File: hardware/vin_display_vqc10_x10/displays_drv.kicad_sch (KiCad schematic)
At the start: 38 parts, among them Q2 DMP2022LSS, Q3 DMP2022LSS, Q4 DMP2022LSS, Q5 DMP2022LSS, Q6 DMP2022LSS, Q8 DMP2022LSS, Q9 DMP2022LSS, U14 74HCT154, U15 74HCT154, U16 74HCT154

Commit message: routing vqc10_x10
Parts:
- removed C28, C29, C30, C31, C32, C38, C39, C40, C41, C42: 0.1u, Capacitor_SMD:C_0603_1608Metric, symbol Device:C
- R14: footprint (none) -> Capacitor_SMD:C_0603_1608Metric
- U14, U15, U16: footprint (none) -> Package_SO:TSSOP-24_4.4x7.8mm_P0.65mm
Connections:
- net DISP_C17: no longer U16.1 (Y0)
- net DISP_C18: no longer U16.2 (Y1)
- net DISP_C19: no longer U16.3 (Y2)
- net DISP_C20: no longer U16.4 (Y3)
- net DISP_C21: no longer U16.5 (Y4)
- net DISP_C22: no longer U16.6 (Y5)
- net DISP_C23: no longer U16.7 (Y6)
- net DISP_C24: no longer U16.8 (Y7)
- new net DISP_C33: U16.1 (Y0)
- new net DISP_C34: U16.2 (Y1)
- new net DISP_C35: U16.3 (Y2)
- new net DISP_C36: U16.4 (Y3)
- new net DISP_C37: U16.5 (Y4)
- new net DISP_C38: U16.6 (Y5)
- new net DISP_C39: U16.7 (Y6)
- new net DISP_C40: U16.8 (Y7)
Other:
- moved on the sheet: C23, C24, C25, C26, C27, C33, C34, C35, C36, C37

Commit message: route vqc10_x10 board
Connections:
- net DISP_VCC: now also U14.24 (VCC), U15.24 (VCC), U16.24 (VCC)
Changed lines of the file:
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@@
   (junction (at 250.19 97.79) (diameter 0) (color 0 0 0 0)
   )
+  (junction (at 63.5 114.3) (diameter 0) (color 0 0 0 0)
+  )
   (junction (at 73.66 84.455) (diameter 0) (color 0 0 0 0)
   )
@@
   )
   (wire (pts (xy 127.635 50.8) (xy 127.635 53.34))
+    (stroke (width 0) (type default))
+  )
+  (wire (pts (xy 63.5 114.3) (xy 78.74 114.3))
     (stroke (width 0) (type default))
   )
@@
       (effects (font (size 1.27 1.27)) (justify left) hide)
     )
+  )
+  (global_label "DISP_VCC" (shape input) (at 78.74 114.3 0) (fields_autoplaced)
+    (effects (font (size 1.27 1.27)) (justify left))
+    (property "Intersheetrefs" "${INTERSHEET_REFS}" (at 90.6757 114.3 0)
+      (effects (font (size 1.27 1.27)) (justify left) hide)
+    )

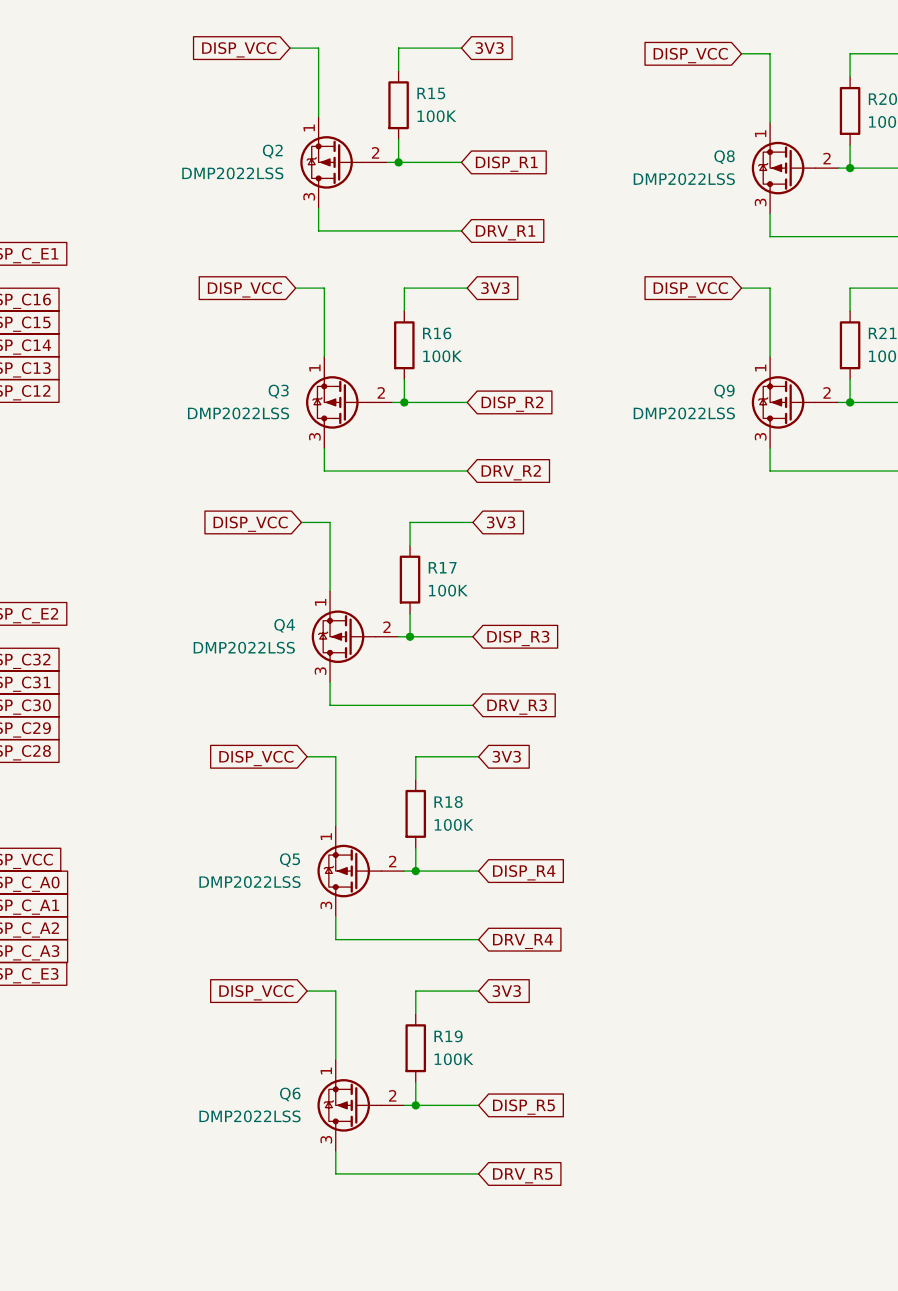
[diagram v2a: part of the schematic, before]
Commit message: minor fixes in vqc10_x10 and hdsp2000_x20 pcb/schematics
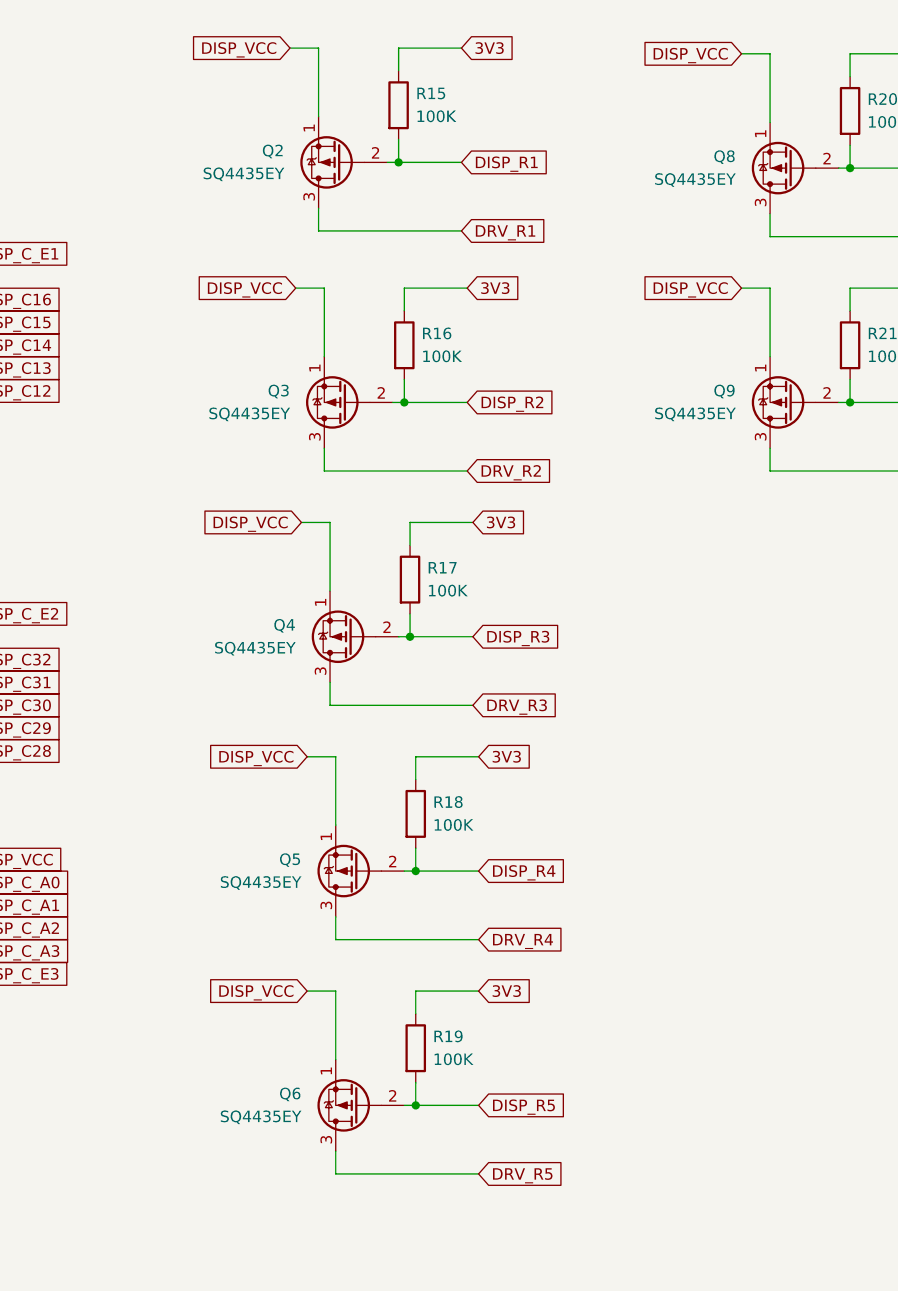
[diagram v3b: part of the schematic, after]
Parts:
- Q2, Q3, Q4, Q5, Q6, Q8, Q9: value DMP2022LSS -> SQ4435EY
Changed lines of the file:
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@@
       (effects (font (size 1.27 1.27)) (justify left))
     )
-    (property "Value" "DMP2022LSS" (at 164.465 38.735 0)
+    (property "Value" "SQ4435EY" (at 164.465 38.735 0)
       (effects (font (size 1.27 1.27)) (justify left))
     )
@@
       (effects (font (size 1.27 1.27)) (justify left))
     )
-    (property "Value" "DMP2022LSS" (at 116.205 116.84 0)
+    (property "Value" "SQ4435EY" (at 116.205 116.84 0)
       (effects (font (size 1.27 1.27)) (justify left))
     )
@@
       (effects (font (size 1.27 1.27)) (justify left))
     )
-    (property "Value" "DMP2022LSS" (at 116.205 142.875 0)
+    (property "Value" "SQ4435EY" (at 116.205 142.875 0)
       (effects (font (size 1.27 1.27)) (justify left))
     )
@@
       (effects (font (size 1.27 1.27)) (justify left))
     )
-    (property "Value" "DMP2022LSS" (at 114.3 38.1 0)
+    (property "Value" "SQ4435EY" (at 114.3 38.1 0)
       (effects (font (size 1.27 1.27)) (justify left))
     )
@@
       (effects (font (size 1.27 1.27)) (justify left))
     )
-    (property "Value" "DMP2022LSS" (at 114.935 64.77 0)
+    (property "Value" "SQ4435EY" (at 114.935 64.77 0)
       (effects (font (size 1.27 1.27)) (justify left))
     )
@@
       (effects (font (size 1.27 1.27)) (justify left))
     )
-    (property "Value" "DMP2022LSS" (at 115.57 90.805 0)
+    (property "Value" "SQ4435EY" (at 115.57 90.805 0)
       (effects (font (size 1.27 1.27)) (justify left))
     )
@@
       (effects (font (size 1.27 1.27)) (justify left))
     )
-    (property "Value" "DMP2022LSS" (at 164.465 64.77 0)
-      (effects (font (size 1.27 1.27)) (justify left))
-    )
+    (property "Value" "SQ4435EY" (at 164.465 64.77 0)
+      (effects (font (size 1.27 1.27)) (justify left))
+    )
